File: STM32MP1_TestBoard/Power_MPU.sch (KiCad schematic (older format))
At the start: 27 parts, among them U5 STM32MP157xAB

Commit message: updated bom, readme
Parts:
- removed U5: STM32MP157xAB, STM32MP151_LFBGA:BGA-361_19x19_16.0x16.0mm, symbol STM32MP151:STM32MP157xAB
- added U1: STM32MP157xAB, STM32MP151_LFBGA:BGA-361_19x19_16.0x16.0mm, symbol STM32MP15x:STM32MP157xAB
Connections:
- wire segments 451 -> 153
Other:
- moved on the sheet: C11, C12, C13, C14, C15, C16, L3

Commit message: swapped smps for ldo
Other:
- moved on the sheet: C11, C12, C13, C14, C15, C16, C17, C18, C19, C20, C21, C22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

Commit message: minor schema updates
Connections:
- net labels added: 1V8_DETECT
- net labels removed: +1V8, 3.3V, 3V3_Delayed
- wire segments 153 -> 152
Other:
- moved on the sheet: C11, C13, C15, C16

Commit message: updated schematic design
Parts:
- removed C11: 100nF, Capacitor_SMD:C_0402_1005Metric_Pad0.74x0.62mm_HandSolder, symbol Device:C
- removed C13, C15, C16: 1uF, Capacitor_SMD:C_0402_1005Metric_Pad0.74x0.62mm_HandSolder, symbol Device:C
- added C68, C70: 1uF, Capacitor_SMD:C_0402_1005Metric_Pad0.74x0.62mm_HandSolder, symbol Device:C
- added C69, C7, C9: 2.2uF, Capacitor_SMD:C_0402_1005Metric_Pad0.74x0.62mm_HandSolder, symbol Device:C
- added JP4: Jumper_NC_Small, Jumper:SolderJumper-2_P1.3mm_Bridged_Pad1.0x1.5mm, symbol Device:Jumper_NC_Small
- C17: value 100nF -> 1uF
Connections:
- net labels added: 1.35V_VDDCORE, 3.3v_VDD, PWR_ON
- net labels removed: +1V35, +3.3V
- wire segments 152 -> 161
- no-connect marks 0 -> 1
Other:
- moved on the sheet: C12, C14, C17, C18, C19, C20, C21, C22, C23, C24, C25, C26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

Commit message: layout update
backup. work in progress
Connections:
- net labels added: 3.3V_VDD
- net labels removed: 3.3v_VDD
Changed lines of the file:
@@
 	4975 3775 6900 3775
 Text HLabel 4725 2825 0    50   Input ~ 0
-3.3v_VDD
+3.3V_VDD
 Wire Wire Line
 	4725 2825 6900 2825
 Text HLabel 11200 2775 2    50   Input ~ 0
-3.3v_VDD
+3.3V_VDD
 Text HLabel 3350 8200 0    50   Input ~ 0
 1.35V_VDDCORE
 Text HLabel 8050 8175 0    50   Input ~ 0
-3.3v_VDD
+3.3V_VDD
 Text HLabel 11825 8175 0    50   Input ~ 0
 1.35V_VDDCORE

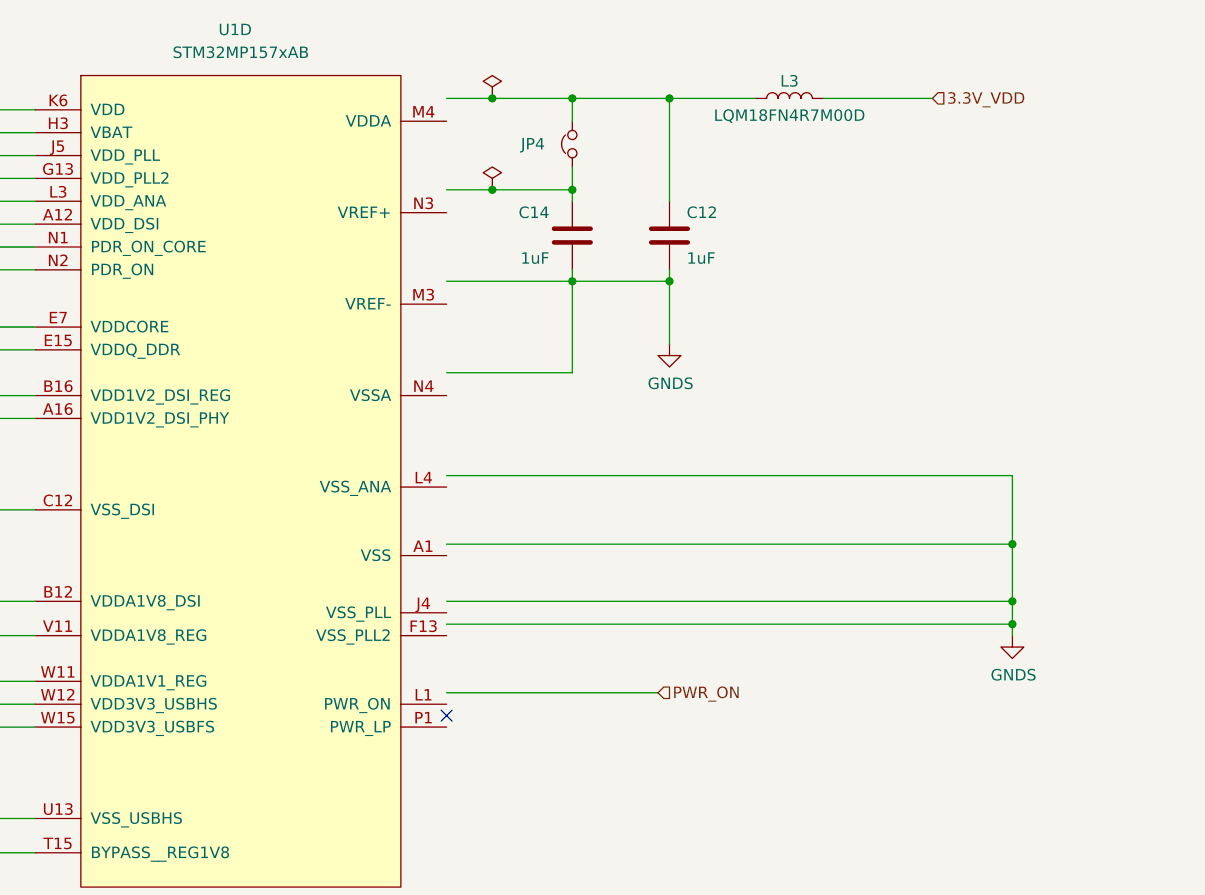
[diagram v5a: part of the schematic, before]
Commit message: updated to use stm32MP15x symbol library
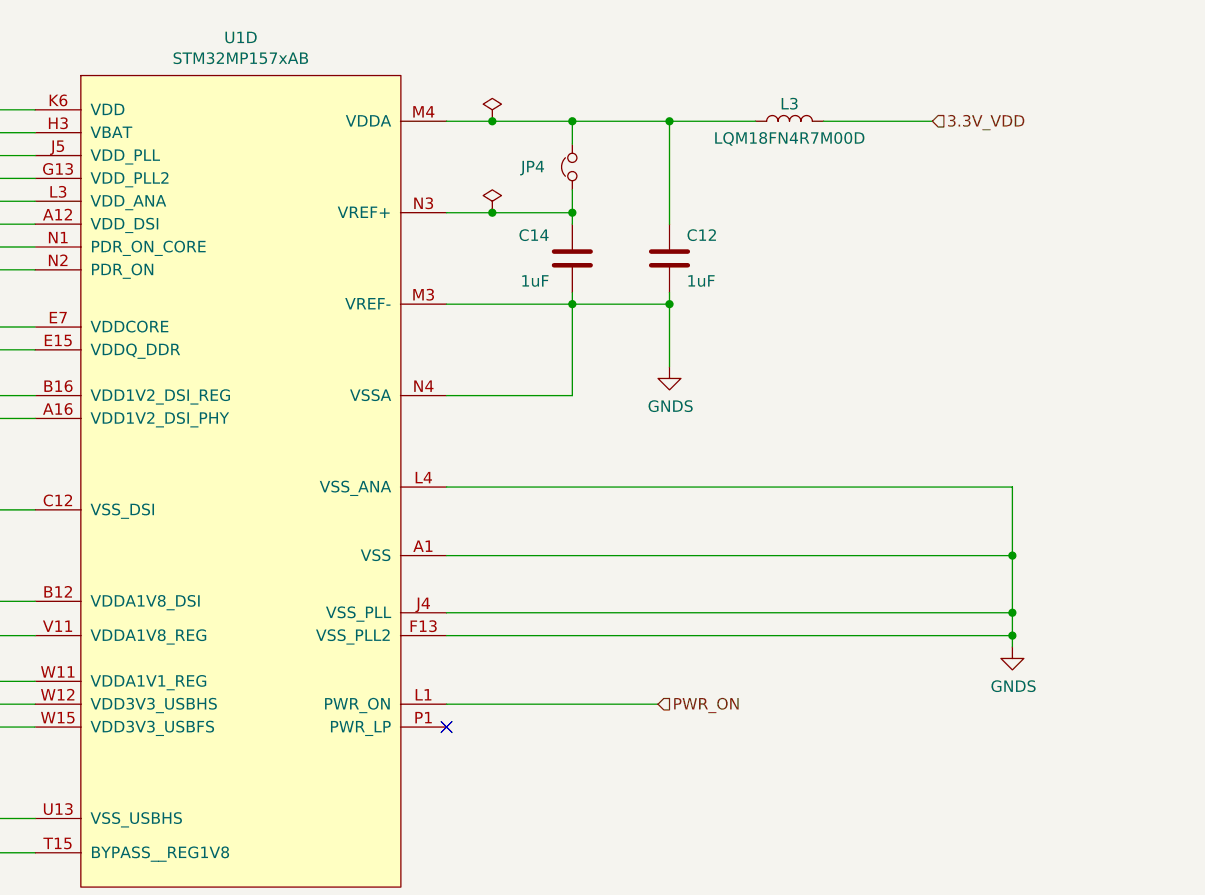
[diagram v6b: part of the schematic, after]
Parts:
- U1: Mfr STMicroelectronics -> (none); PartNo STM32MP157FAB -> (none)
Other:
- moved on the sheet: C12, C14, JP4, L3
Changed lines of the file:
@@
 L power:GNDS #PWR?
 U 1 1 6046CE0A
-P 11550 5125
+P 11550 5175
 AR Path="/6046CE0A" Ref="#PWR?"  Part="1"
 AR Path="/6044C48A/6046CE0A" Ref="#PWR026"  Part="1"
-F 0 "#PWR026" H 11550 4875 50  0001 C CNN
-F 1 "GNDS" H 11555 4952 50  0000 C CNN
-F 2 "" H 11550 5125 50  0001 C CNN
-F 3 "" H 11550 5125 50  0001 C CNN
-	1    11550 5125
+F 0 "#PWR026" H 11550 4925 50  0001 C CNN
+F 1 "GNDS" H 11555 5002 50  0000 C CNN
+F 2 "" H 11550 5175 50  0001 C CNN
+F 3 "" H 11550 5175 50  0001 C CNN
+	1    11550 5175
 	1    0    0    -1
 $EndComp
@@
 	7275 5425 7050 5425
 $Comp
-L STM32MP15x:STM32MP157xAB U1
-U 4 1 5FD1B3DF
-P 8175 4425
-F 0 "U1" H 8150 6375 50  0000 C CNN
-F 1 "STM32MP157xAB" H 8175 6275 50  0000 C CNN
-F 2 "STM32MP151_LFBGA:BGA-361_19x19_16.0x16.0mm" H 8075 9675 50  0001 C CNN
-F 3 "https://www.st.com/resource/en/datasheet/stm32mp157f.pdf" H 8425 7575 50  0001 C CNN
-F 4 "STMicroelectronics" H 8175 4425 50  0001 C CNN "Mfr"
-F 5 "STM32MP157FAB" H 8175 4425 50  0001 C CNN "PartNo"
-	4    8175 4425
-	1    0    0    -1
-$EndComp
-$Comp
 L Device:L L?
 U 1 1 6046CF1F
-P 10575 2775
+P 10575 2875
 AR Path="/6046CF1F" Ref="L?"  Part="1"
 AR Path="/6044C48A/6046CF1F" Ref="L3"  Part="1"
-F 0 "L3" V 10650 2775 50  0000 C CNN
-F 1 "LQM18FN4R7M00D " V 10500 2775 50  0000 C CNN
-F 2 "Inductor_SMD:L_0201_0603Metric_Pad0.64x0.40mm_HandSolder" H 10575 2775 50  0001 C CNN
-F 3 "https://www.mouser.co.uk/datasheet/2/281/JELF243B-0012-1633801.pdf" H 10575 2775 50  0001 C CNN
-F 4 "~" H 10575 2775 50  0001 C CNN "Mfr"
-F 5 "~" H 10575 2775 50  0001 C CNN "PartNo"
-	1    10575 2775
+F 0 "L3" V 10650 2875 50  0000 C CNN
+F 1 "LQM18FN4R7M00D " V 10500 2875 50  0000 C CNN
+F 2 "Inductor_SMD:L_0201_0603Metric_Pad0.64x0.40mm_HandSolder" H 10575 2875 50  0001 C CNN
+F 3 "https://www.mouser.co.uk/datasheet/2/281/JELF243B-0012-1633801.pdf" H 10575 2875 50  0001 C CNN
+F 4 "~" H 10575 2875 50  0001 C CNN "Mfr"
+F 5 "~" H 10575 2875 50  0001 C CNN "PartNo"
+	1    10575 2875
 	0    1    -1   0
 $EndComp
@@
 L Device:C C?
 U 1 1 6046CF55
-P 9625 3375
+P 9625 3475
 AR Path="/6046CF55" Ref="C?"  Part="1"
 AR Path="/6044C48A/6046CF55" Ref="C14"  Part="1"
-F 0 "C14" H 9725 3275 50  0000 L CNN
-F 1 "1uF" H 9725 3475 50  0000 L CNN
-F 2 "Capacitor_SMD:C_0402_1005Metric_Pad0.74x0.62mm_HandSolder" H 9663 3225 50  0001 C CNN
-F 3 "https://datasheet.lcsc.com/szlcsc/1810201223_Taiyo-Yuden-LMK105BJ105KV-F_C87145.pdf" H 9625 3375 50  0001 C CNN
-F 4 "Taiyo Yuden" H 9625 3375 50  0001 C CNN "Mfr"
-F 5 "LMK105BJ105KV-F" H 9625 3375 50  0001 C CNN "PartNo"
-	1    9625 3375
+F 0 "C14" H 9725 3375 50  0000 L CNN
+F 1 "1uF" H 9725 3575 50  0000 L CNN
+F 2 "Capacitor_SMD:C_0402_1005Metric_Pad0.74x0.62mm_HandSolder" H 9663 3325 50  0001 C CNN
+F 3 "https://datasheet.lcsc.com/szlcsc/1810201223_Taiyo-Yuden-LMK105BJ105KV-F_C87145.pdf" H 9625 3475 50  0001 C CNN
+F 4 "Taiyo Yuden" H 9625 3475 50  0001 C CNN "Mfr"
+F 5 "LMK105BJ105KV-F" H 9625 3475 50  0001 C CNN "PartNo"
+	1    9625 3475
 	-1   0    0    1
 $EndComp
@@
 L Device:C C?
 U 1 1 6046CF3F
-P 10050 3375
+P 10050 3475
 AR Path="/6046CF3F" Ref="C?"  Part="1"
 AR Path="/6044C48A/6046CF3F" Ref="C12"  Part="1"
-F 0 "C12" H 10125 3275 50  0000 L CNN
-F 1 "1uF" H 10125 3475 50  0000 L CNN
-F 2 "Capacitor_SMD:C_0402_1005Metric_Pad0.74x0.62mm_HandSolder" H 10088 3225 50  0001 C CNN
-F 3 "https://datasheet.lcsc.com/szlcsc/1810201223_Taiyo-Yuden-LMK105BJ105KV-F_C87145.pdf" H 10050 3375 50  0001 C CNN
-F 4 "Taiyo Yuden" H 10050 3375 50  0001 C CNN "Mfr"
-F 5 "LMK105BJ105KV-F" H 10050 3375 50  0001 C CNN "PartNo"
-	1    10050 3375
+F 0 "C12" H 10125 3375 50  0000 L CNN
+F 1 "1uF" H 10125 3575 50  0000 L CNN
+F 2 "Capacitor_SMD:C_0402_1005Metric_Pad0.74x0.62mm_HandSolder" H 10088 3325 50  0001 C CNN
+F 3 "https://datasheet.lcsc.com/szlcsc/1810201223_Taiyo-Yuden-LMK105BJ105KV-F_C87145.pdf" H 10050 3475 50  0001 C CNN
+F 4 "Taiyo Yuden" H 10050 3475 50  0001 C CNN "Mfr"
+F 5 "LMK105BJ105KV-F" H 10050 3475 50  0001 C CNN "PartNo"
+	1    10050 3475
 	1    0    0    1
 $EndComp
@@
 	7275 2825 6900 2825
 Wire Wire Line
-	9075 4425 11550 4425
+	9075 4475 11550 4475
 Wire Wire Line
 	7275 3225 6900 3225
@@
 L power:GNDS #PWR06
 U 1 1 5FCDEAA5
-P 10050 3850
-F 0 "#PWR06" H 10050 3600 50  0001 C CNN
-F 1 "GNDS" H 10055 3677 50  0000 C CNN
-F 2 "" H 10050 3850 50  0001 C CNN
-F 3 "" H 10050 3850 50  0001 C CNN
-	1    10050 3850
-	1    0    0    -1
-$EndComp
-Wire Wire Line
-	9075 3975 9625 3975
-Wire Wire Line
-	9625 3975 9625 3575
-Wire Wire Line
-	9625 3575 9075 3575
-Wire Wire Line
-	9625 3525 9625 3575
-Connection ~ 9625 3575
-Wire Wire Line
-	9625 3225 9625 3175
-Wire Wire Line
-	9625 3175 9275 3175
-Wire Wire Line
-	9625 3575 10050 3575
-Wire Wire Line
-	10050 3575 10050 3525
-Wire Wire Line
-	10050 3850 10050 3575
-Connection ~ 10050 3575
-Wire Wire Line
-	10050 3225 10050 2775
-Connection ~ 10050 2775
-Wire Wire Line
-	10050 2775 10425 2775
-Wire Wire Line
-	10725 2775 11200 2775
-Wire Wire Line
-	9075 2775 9275 2775
+P 10050 3950
+F 0 "#PWR06" H 10050 3700 50  0001 C CNN
+F 1 "GNDS" H 10055 3777 50  0000 C CNN
+F 2 "" H 10050 3950 50  0001 C CNN
+F 3 "" H 10050 3950 50  0001 C CNN
+	1    10050 3950
+	1    0    0    -1
+$EndComp
+Wire Wire Line
+	9075 4075 9625 4075
+Wire Wire Line
+	9625 4075 9625 3675
+Wire Wire Line
+	9625 3675 9075 3675
+Wire Wire Line
+	9625 3625 9625 3675
+Connection ~ 9625 3675
+Wire Wire Line
+	9625 3325 9625 3275
+Wire Wire Line
+	9625 3275 9275 3275
+Wire Wire Line
+	9625 3675 10050 3675
+Wire Wire Line
+	10050 3675 10050 3625
+Wire Wire Line
+	10050 3950 10050 3675
+Connection ~ 10050 3675
+Wire Wire Line
+	10050 3325 10050 2875
+Connection ~ 10050 2875
+Wire Wire Line
+	10050 2875 10425 2875
+Wire Wire Line
+	10725 2875 11200 2875
+Wire Wire Line
+	9075 2875 9275 2875
 $Comp
 L Device:Jumper_NC_Small JP4
 U 1 1 5FDCA779
-P 9625 2975
-F 0 "JP4" V 9625 3200 50  0000 R CNN
-F 1 "Jumper_NC_Small" V 9670 3049 50  0001 L CNN
-F 2 "Jumper:SolderJumper-2_P1.3mm_Bridged_Pad1.0x1.5mm" H 9625 2975 50  0001 C CNN
-F 3 "~" H 9625 2975 50  0001 C CNN
-	1    9625 2975
+P 9625 3075
+F 0 "JP4" V 9625 3300 50  0000 R CNN
+F 1 "Jumper_NC_Small" V 9670 3149 50  0001 L CNN
+F 2 "Jumper:SolderJumper-2_P1.3mm_Bridged_Pad1.0x1.5mm" H 9625 3075 50  0001 C CNN
+F 3 "~" H 9625 3075 50  0001 C CNN
+	1    9625 3075
 	0    -1   -1   0
 $EndComp
 Wire Wire Line
-	9625 2875 9625 2775
-Connection ~ 9625 2775
-Wire Wire Line
-	9625 2775 10050 2775
-Wire Wire Line
-	9625 3075 9625 3175
-Connection ~ 9625 3175
+	9625 2975 9625 2875
+Connection ~ 9625 2875
+Wire Wire Line
+	9625 2875 10050 2875
+Wire Wire Line
+	9625 3175 9625 3275
+Connection ~ 9625 3275
 Wire Wire Line
 	7275 3025 6900 3025
@@
 Connection ~ 5525 5925
 Wire Wire Line
-	11550 4425 11550 4725
-Wire Wire Line
-	9075 4725 11550 4725
-Connection ~ 11550 4725
-Wire Wire Line
-	11550 4725 11550 4975
-Wire Wire Line
-	9075 4975 11550 4975
-Connection ~ 11550 4975
-Wire Wire Line
-	11550 4975 11550 5075
-Wire Wire Line
-	9075 5075 11550 5075
-Connection ~ 11550 5075
-Wire Wire Line
-	11550 5075 11550 5125
+	11550 4475 11550 4775
+Wire Wire Line
+	9075 4775 11550 4775
+Connection ~ 11550 4775
+Wire Wire Line
+	11550 4775 11550 5025
+Wire Wire Line
+	9075 5025 11550 5025
+Connection ~ 11550 5025
+Wire Wire Line
+	11550 5025 11550 5125
+Wire Wire Line
+	9075 5125 11550 5125
+Connection ~ 11550 5125
+Wire Wire Line
+	11550 5125 11550 5175
 $Comp
 L power:PWR_FLAG #FLG0103
 U 1 1 6035EA89
-P 9275 2775
-F 0 "#FLG0103" H 9275 2850 50  0001 C CNN
-F 1 "PWR_FLAG" H 9275 2948 50  0001 C CNN
-F 2 "" H 9275 2775 50  0001 C CNN
-F 3 "~" H 9275 2775 50  0001 C CNN
-	1    9275 2775
-	1    0    0    -1
-$EndComp
-Connection ~ 9275 2775
-Wire Wire Line
-	9275 2775 9625 2775
+P 9275 2875
+F 0 "#FLG0103" H 9275 2950 50  0001 C CNN
+F 1 "PWR_FLAG" H 9275 3048 50  0001 C CNN
+F 2 "" H 9275 2875 50  0001 C CNN
+F 3 "~" H 9275 2875 50  0001 C CNN
+	1    9275 2875
+	1    0    0    -1
+$EndComp
+Connection ~ 9275 2875
+Wire Wire Line
+	9275 2875 9625 2875
 $Comp
 L power:PWR_FLAG #FLG0105
 U 1 1 60360711
-P 9275 3175
-F 0 "#FLG0105" H 9275 3250 50  0001 C CNN
-F 1 "PWR_FLAG" H 9275 3348 50  0001 C CNN
-F 2 "" H 9275 3175 50  0001 C CNN
-F 3 "~" H 9275 3175 50  0001 C CNN
-	1    9275 3175
-	1    0    0    -1
-$EndComp
-Connection ~ 9275 3175
-Wire Wire Line
-	9275 3175 9075 3175
+P 9275 3275
+F 0 "#FLG0105" H 9275 3350 50  0001 C CNN
+F 1 "PWR_FLAG" H 9275 3448 50  0001 C CNN
+F 2 "" H 9275 3275 50  0001 C CNN
+F 3 "~" H 9275 3275 50  0001 C CNN
+	1    9275 3275
+	1    0    0    -1
+$EndComp
+Connection ~ 9275 3275
+Wire Wire Line
+	9275 3275 9075 3275
 $Comp
 L power:PWR_FLAG #FLG0106
@@
 Connection ~ 5175 5125
 Wire Wire Line
-	9075 5375 10000 5375
-Text HLabel 10000 5375 2    50   Input ~ 0
+	9075 5425 10000 5425
+Text HLabel 10000 5425 2    50   Input ~ 0
 PWR_ON
-NoConn ~ 9075 5475
+NoConn ~ 9075 5525
 Wire Wire Line
 	7275 3525 6900 3525
@@
 Wire Wire Line
 	4725 2825 6900 2825
-Text HLabel 11200 2775 2    50   Input ~ 0
+Text HLabel 11200 2875 2    50   Input ~ 0
 3.3V_VDD
 Text HLabel 3350 8200 0    50   Input ~ 0
@@
 Text HLabel 11825 8175 0    50   Input ~ 0
 1.35V_VDDCORE
+$Comp
+L STM32MP15x:STM32MP157xAB U1
+U 4 1 5FB9A366
+P 8175 4425
+F 0 "U1" H 8175 6340 50  0000 C CNN
+F 1 "STM32MP157xAB" H 8175 6249 50  0000 C CNN
+F 2 "STM32MP151_LFBGA:BGA-361_19x19_16.0x16.0mm" H 8025 6325 50  0001 C CNN
+F 3 "https://www.st.com/resource/en/datasheet/stm32mp151c.pdf" H 8825 4575 50  0001 C CNN
+	4    8175 4425
+	1    0    0    -1
+$EndComp
 $EndSCHEMATC

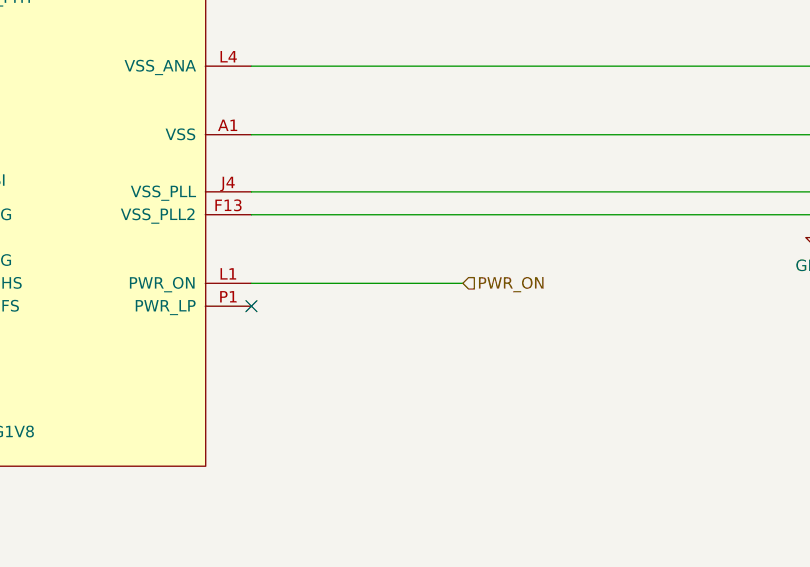
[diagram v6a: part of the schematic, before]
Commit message: swapped DDR3 high/low strobe diff pairs
- corrected DRC errors
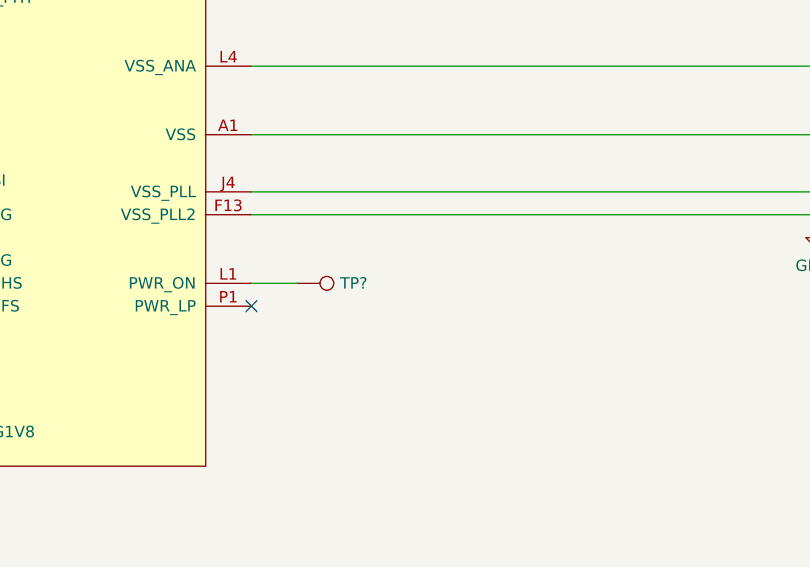
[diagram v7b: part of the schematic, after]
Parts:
- added TP?: TestPoint, TestPoint:TestPoint_Pad_D1.0mm, symbol Connector:TestPoint
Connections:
- net PWR_ON: no longer names the net of U1.L1 (PWR_ON)
- net PWR_ON: now also TP?.1
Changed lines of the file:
@@
 	6100 4075 5525 4075
 Connection ~ 5175 5125
-Wire Wire Line
-	9075 5425 10000 5425
-Text HLabel 10000 5425 2    50   Input ~ 0
-PWR_ON
 NoConn ~ 9075 5525
 Wire Wire Line
@@
 	1    0    0    -1
 $EndComp
+$Comp
+L Connector:TestPoint TP?
+U 1 1 5FCFAF5B
+P 9275 5425
+F 0 "TP?" V 9275 5613 50  0000 L CNN
+F 1 "TestPoint" V 9320 5613 50  0001 L CNN
+F 2 "TestPoint:TestPoint_Pad_D1.0mm" H 9475 5425 50  0001 C CNN
+F 3 "~" H 9475 5425 50  0001 C CNN
+	1    9275 5425
+	0    1    1    0
+$EndComp
+Wire Wire Line
+	9075 5425 9275 5425
 $EndSCHEMATC

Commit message: updates
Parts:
- gave numbers to parts that had none: 1
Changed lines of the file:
@@
 $EndComp
 $Comp
-L Connector:TestPoint TP?
+L Connector:TestPoint TP1
 U 1 1 5FCFAF5B
 P 9275 5425
-F 0 "TP?" V 9275 5613 50  0000 L CNN
+F 0 "TP1" V 9275 5613 50  0000 L CNN
 F 1 "TestPoint" V 9320 5613 50  0001 L CNN
 F 2 "TestPoint:TestPoint_Pad_D1.0mm" H 9475 5425 50  0001 C CNN
